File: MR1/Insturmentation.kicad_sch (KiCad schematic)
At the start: 40 parts, among them J1 Conn_01x01_Pin, J10 Conn_01x01_Pin, J11 Conn_01x01_Pin, J12 Conn_01x10, J2 Conn_01x01_Pin, J9 Conn_01x10, U10 AD40xxBRMZ, U16 LTC6268xS8, U2 LMP7721, U6 ADA4940-1xCP

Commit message: Signed-off-by: lokimetasmith <lokimail@gmail.com>
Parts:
- added C34: 100nF, Capacitor_SMD:C_0402_1005Metric, symbol Device:C
- added C41: 1nF, Capacitor_SMD:C_0402_1005Metric, symbol Device:C_Small
- added J13, J14: Conn_01x10, Connector_JST:JST_SH_SM10B-SRSS-TB_1x10-1MP_P1.00mm_Horizontal, symbol MR1:Conn_01x11_MP
- added U11: LP5907MFX-1.8, Package_TO_SOT_SMD:SOT-23-5, symbol Regulator_Linear:LP5907MFX-1.8
- C29, C30: value 10nF -> 10pF
- R43, R44, R45, R46: value 1K -> 499 (0.1%)
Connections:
- net +1V8: now also C34.1, U11.5 (OUT)
- net +3V3: now also J14.2 (Pin_2), U11.1 (IN), U11.3 (EN)
- net DAC_CLK: now also J14.4 (Pin_4)
- net DAC_SDI: now also J14.6 (Pin_6)
- net DAC_SDO: now also J14.5 (Pin_5)
- net GNDA: now also J14.10 (Pin_10), J14.8 (Pin_8)
- net VDDA: now also J14.9 (Pin_9)
- net VSSA: now also J14.7 (Pin_7)
- net at C30.1, R41.2, U10.4 (IN-): now also C41.2
- net at C29.2, R27.2, U10.3 (IN+): now also C41.1
- new net GND: C34.2, J14.3 (Pin_3), U11.2 (GND)
- no-connect marks 0 -> 1
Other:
- moved on the sheet: C31, C32, C33, C35, J12, J9, U10, U6B

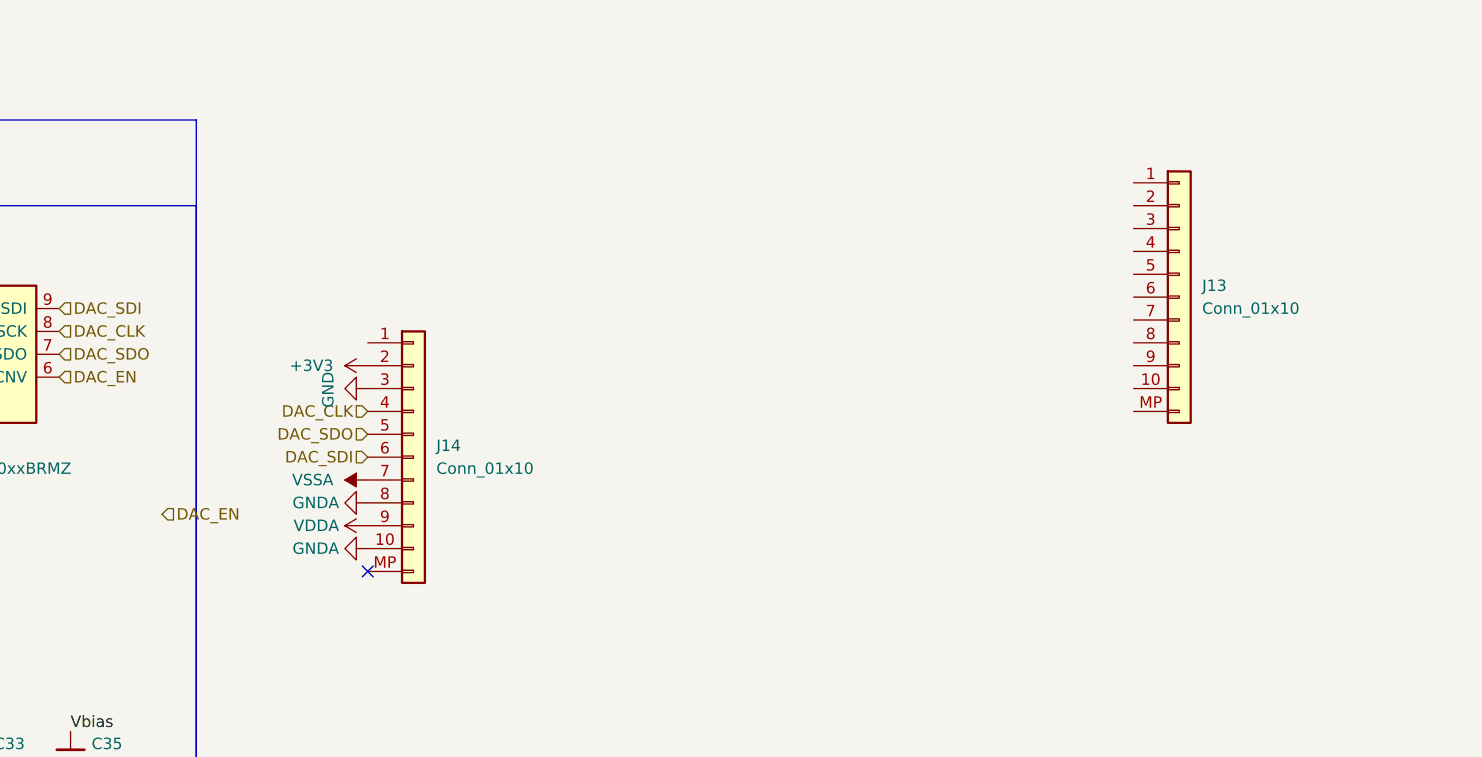
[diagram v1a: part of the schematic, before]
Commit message: feat(cad,firmware,interposer): PTFE interposer, deliverables pipeline, and firmware
- CAD & Interposer:
  - Modeled PTFE_Interposer (55.0 x 51.962 x 0.8 mm) with central wafer diamond cutout
  - Dual-sided silver chloride (Ag/AgCl) ribbon electrode pads (30 deg Cis, 210 deg Trans)
  - 6-pad pogo pin landing array and 4 fluidic pass-throughs with weep duct relief
  - Verified 0 physical collisions across cartridge stack and housings (100% green)
- Deliverables & Export Pipeline:
  - Created automated export system (Makefile, scripts/export_manager.py, scripts/export_all.sh)
  - Full cataloging of 159 deliverables (30 STLs, 13 DXFs, STEPs, Gerbers, WireViz)
  - Added E2E tests (tests/test_exports_e2e.py) and legacy parity tests (tests/test_legacy_feature_parity.py)
- Firmware & Schematics:
  - ESP32-S3 firmware with 100 kHz USB streaming, FreeRTOS dual-core tasks, Web UI
  - Added fast AD40xx SPI driver, MCP4822 DAC driver, leak detection, and pump UART
  - SBU auto-polarity detection and I2C routing in MR1 schematics
- Docs & Environment:
  - Added setup_env.sh, setup_env.ps1, requirements.txt, EXPORTS.md
  - Updated README.md, TODO.md, atlas.project.json, and walkthrough.md
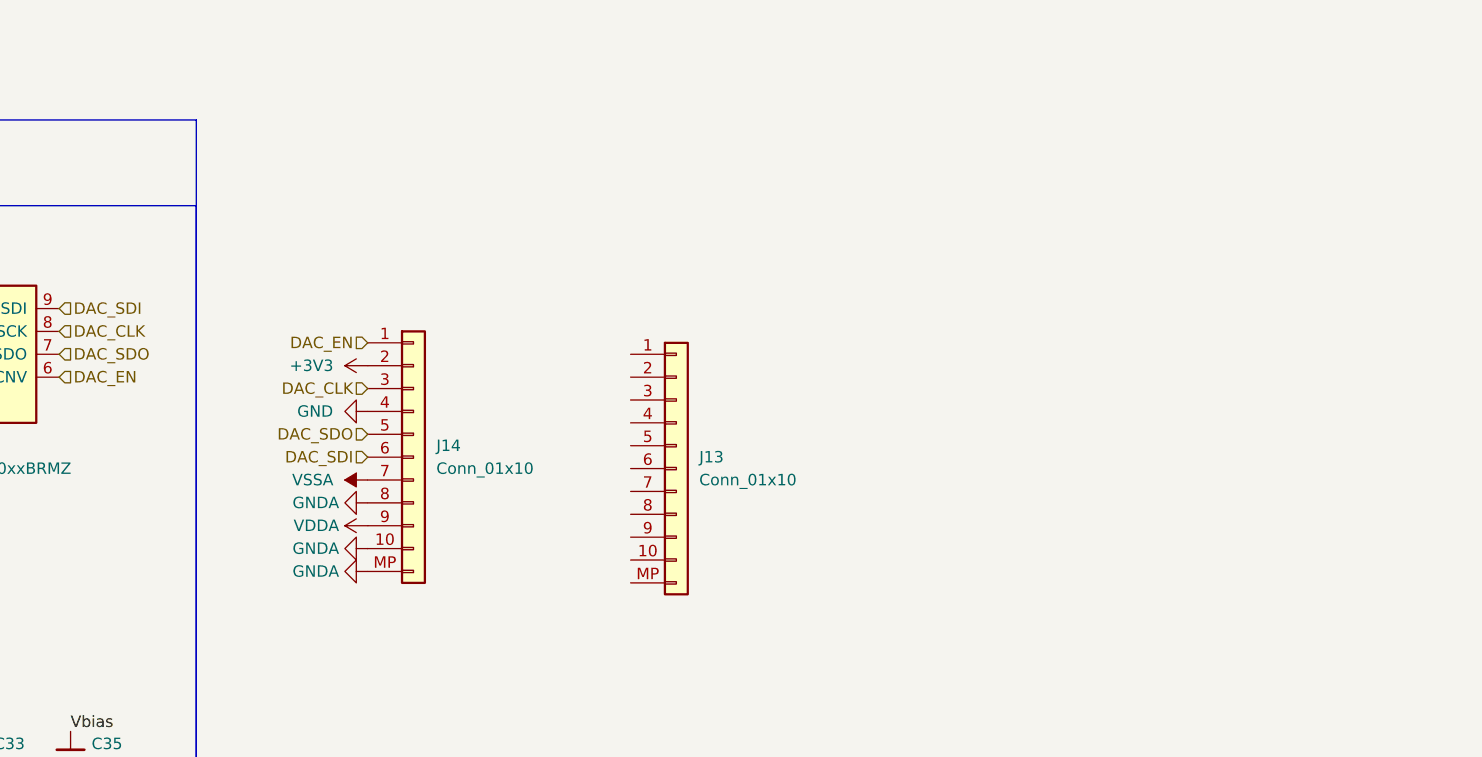
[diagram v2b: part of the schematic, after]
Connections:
- net DAC_CLK: now also J14.3 (Pin_3); no longer J14.4 (Pin_4)
- net DAC_EN: now also J14.1 (Pin_1)
- net GND: now also J14.4 (Pin_4); no longer J14.3 (Pin_3)
- net GNDA: now also J14.MP (Pin_11)
- no-connect marks 1 -> 0
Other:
- moved on the sheet: J13
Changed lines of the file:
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@@
 		(color 0 0 0 0)
 	)
-	(no_connect
-		(at 267.97 63.5)
-	)
 	(wire
 		(pts
@@
 	(hierarchical_label "DAC_EN"
 		(shape input)
-		(at 245.11 57.15 0)
+		(at 267.97 38.1 180)
 		(effects
 			(font
 				(size 1.27 1.27)
 			)
-			(justify left)
+			(justify right)
 		)
 	)
@@
 	(hierarchical_label "DAC_CLK"
 		(shape input)
-		(at 267.97 45.72 180)
+		(at 267.97 43.18 180)
 		(effects
 			(font
@@
 	(symbol
 		(lib_id "temp-sensor-rescue:GND-power-temp-sensor-rescue")
-		(at 267.97 43.18 270)
+		(at 267.97 45.72 270)
 		(unit 1)
 		(body_style 1)
@@
 		(dnp no)
 		(property "Reference" "#PWR0136"
-			(at 261.62 43.18 0)
+			(at 261.62 45.72 0)
 			(hide yes)
 			(show_name no)
@@
 		)
 		(property "Value" "GND"
-			(at 263.5758 43.307 0)
+			(at 262.128 45.72 90)
 			(show_name no)
 			(do_not_autoplace no)
@@
 		)
 		(property "Footprint" ""
-			(at 267.97 43.18 0)
+			(at 267.97 45.72 0)
 			(hide yes)
 			(show_name no)
@@
 		)
 		(property "Datasheet" ""
-			(at 267.97 43.18 0)
+			(at 267.97 45.72 0)
 			(hide yes)
 			(show_name no)
@@
 		)
 		(property "Description" ""
-			(at 267.97 43.18 0)
+			(at 267.97 45.72 0)
 			(show_name no)
 			(do_not_autoplace no)
@@
 	)
 	(symbol
+		(lib_id "power:GNDA")
+		(at 267.97 63.5 270)
+		(unit 1)
+		(body_style 1)
+		(exclude_from_sim no)
+		(in_bom yes)
+		(on_board yes)
+		(in_pos_files yes)
+		(dnp no)
+		(fields_autoplaced yes)
+		(property "Reference" "#PWR0137"
+			(at 261.62 63.5 0)
+			(hide yes)
+			(show_name no)
+			(do_not_autoplace no)
+			(effects
+				(font
+					(size 1.27 1.27)
+				)
+			)
+		)
+		(property "Value" "GNDA"
+			(at 264.795 63.4999 90)
+			(show_name no)
+			(do_not_autoplace no)
+			(effects
+				(font
+					(size 1.27 1.27)
+				)
+				(justify right)
+			)
+		)
+		(property "Footprint" ""
+			(at 267.97 63.5 0)
+			(hide yes)
+			(show_name no)
+			(do_not_autoplace no)
+			(effects
+				(font
+					(size 1.27 1.27)
+				)
+			)
+		)
+		(property "Datasheet" ""
+			(at 267.97 63.5 0)
+			(hide yes)
+			(show_name no)
+			(do_not_autoplace no)
+			(effects
+				(font
+					(size 1.27 1.27)
+				)
+			)
+		)
+		(property "Description" "Power symbol creates a global label with name \"GNDA\" , analog ground"
+			(at 267.97 63.5 0)
+			(hide yes)
+			(show_name no)
+			(do_not_autoplace no)
+			(effects
+				(font
+					(size 1.27 1.27)
+				)
+			)
+		)
+		(pin "1"
+		)
+		(instances
+			(project "MR1"
+				(path "/0fac162c-ca5e-4358-934a-30718aa12176/38d1a3ed-811f-4f3b-80a2-5ae77b649a51"
+					(reference "#PWR0137")
+					(unit 1)
+				)
+			)
+		)
+	)
+	(symbol
 		(lib_id "Device:C")
 		(at 113.03 64.77 0)
@@
 	(symbol
 		(lib_id "MR1:Conn_01x11_MP")
-		(at 358.14 33.02 0)
+		(at 302.26 52.07 0)
 		(unit 1)
 		(body_style 1)
@@
 		(fields_autoplaced yes)
 		(property "Reference" "J13"
-			(at 360.68 31.7499 0)
+			(at 304.8 50.7999 0)
 			(show_name no)
 			(do_not_autoplace no)
@@
 		)
 		(property "Value" "Conn_01x10"
-			(at 360.68 34.2899 0)
+			(at 304.8 53.3399 0)
 			(show_name no)
 			(do_not_autoplace no)
@@
 		)
 		(property "Footprint" "Connector_JST:JST_SH_SM10B-SRSS-TB_1x10-1MP_P1.00mm_Horizontal"
-			(at 358.14 33.02 0)
+			(at 302.26 52.07 0)
 			(hide yes)
 			(show_name no)
@@
 		)
 		(property "Datasheet" ""
-			(at 358.14 33.02 0)
+			(at 302.26 52.07 0)
 			(hide yes)
 			(show_name no)
@@
 		)
 		(property "Description" "Generic connector, single row, 01x11, script generated (kicad-library-utils/schlib/autogen/connector/)"
-			(at 358.14 33.02 0)
+			(at 302.26 52.07 0)
 			(hide yes)
 			(show_name no)

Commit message: commiting pcb changes
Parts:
- removed C1: 2pF, Capacitor_SMD:C_0402_1005Metric, symbol Device:C
- removed C19, C20, C34, C6: 100nF, Capacitor_SMD:C_0402_1005Metric, symbol Device:C
- removed C29, C30: 10pF, Capacitor_SMD:C_0402_1005Metric, symbol Device:C
- removed C35: 10u, Capacitor_SMD:C_0402_1005Metric, symbol Device:C_Small
- removed C41: 1nF, Capacitor_SMD:C_0402_1005Metric, symbol Device:C_Small
- removed H1: Nanopore, footprints:Nanopore holder_recessed, symbol Mechanical:MountingHole
- removed J1, J10, J11, J2: Conn_01x01_Pin, footprints:Electrode, symbol Connector:Conn_01x01_Pin
- removed J12, J13, J14, J9: Conn_01x10, Connector_JST:JST_SH_SM10B-SRSS-TB_1x10-1MP_P1.00mm_Horizontal, symbol MR1:Conn_01x11_MP
- removed NT3: NetTie_2, NetTie:NetTie-2_SMD_Pad0.5mm, symbol Device:NetTie_2
- removed R1: 1M, Resistor_SMD:R_0402_1005Metric, symbol Device:R
- removed R27, R41: 27, Resistor_SMD:R_0402_1005Metric, symbol Device:R_Small_US
- removed R3, R5, R6: 1K, Resistor_SMD:R_0402_1005Metric, symbol Device:R
- removed R4, R8: 100, Resistor_SMD:R_0402_1005Metric, symbol Device:R
- removed R43, R44, R45, R46: 499 (0.1%), Resistor_SMD:R_0402_1005Metric, symbol Device:R
- removed U10: AD40xxBRMZ, Package_SO:MSOP-10_3x3mm_P0.5mm, symbol Analog_ADC:AD40xxBRMZ
- removed U11: LP5907MFX-1.8, Package_TO_SOT_SMD:SOT-23-5, symbol Regulator_Linear:LP5907MFX-1.8
- removed U16: LTC6268xS8, Package_SO:SO-8_3.9x4.9mm_P1.27mm, symbol MR1:LTC6268xS8-10_SHIELD
- removed U2: LMP7721, Package_SO:SOIC-8_3.9x4.9mm_P1.27mm, symbol LMP7721:LMP7721
- removed U6: ADA4940-1xCP, Package_CSP:LFCSP-16-1EP_3x3mm_P0.5mm_EP1.3x1.3mm_ThermalVias, symbol Amplifier_Difference:ADA4940-1xCP
- added J7: Conn_01x14_MountingPin, Connector_FFC-FPC:Amphenol_F32R-1A7x1-11014_1x14-1MP_P0.5mm_Horizontal, symbol Connector_Generic_MountingPin:Conn_01x14_MountingPin
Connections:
- net +3V3: now also J7.1 (Pin_1)
- net >PORE: now also J7.14 (Pin_14)
- net GND: now also J7.2 (Pin_2), J7.4 (Pin_4), J7.8 (Pin_8)
- net GNDA: now also J7.11 (Pin_11), J7.13 (Pin_13), J7.9 (Pin_9)
- net SHIELD: now also J7.MP (MountPin)
- net VDDA: now also J7.10 (Pin_10)
- net VSSA: now also J7.12 (Pin_12)
- new net ADC_CLK: J7.3 (Pin_3)
- new net ADC_EN: J7.6 (Pin_6)
- new net ADC_SDI: J7.7 (Pin_7)
- new net ADC_SDO: J7.5 (Pin_5)
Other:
- note removed: "499Ω Metal Film Resistor"
- note removed: "LTC6268"
- note removed: "P1"
- note removed: "P2"
- note removed: "P3"
- note removed: "P4"
- note removed: "R1 1206"
- note removed: "Stage 2 Voltage Amplifier"
- note removed: "Virtual Ground"
- note removed: "low noise voltage converters"
- moved on the sheet: C2, C3, C33, C4, C5
